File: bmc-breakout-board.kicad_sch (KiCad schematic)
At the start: 9 parts

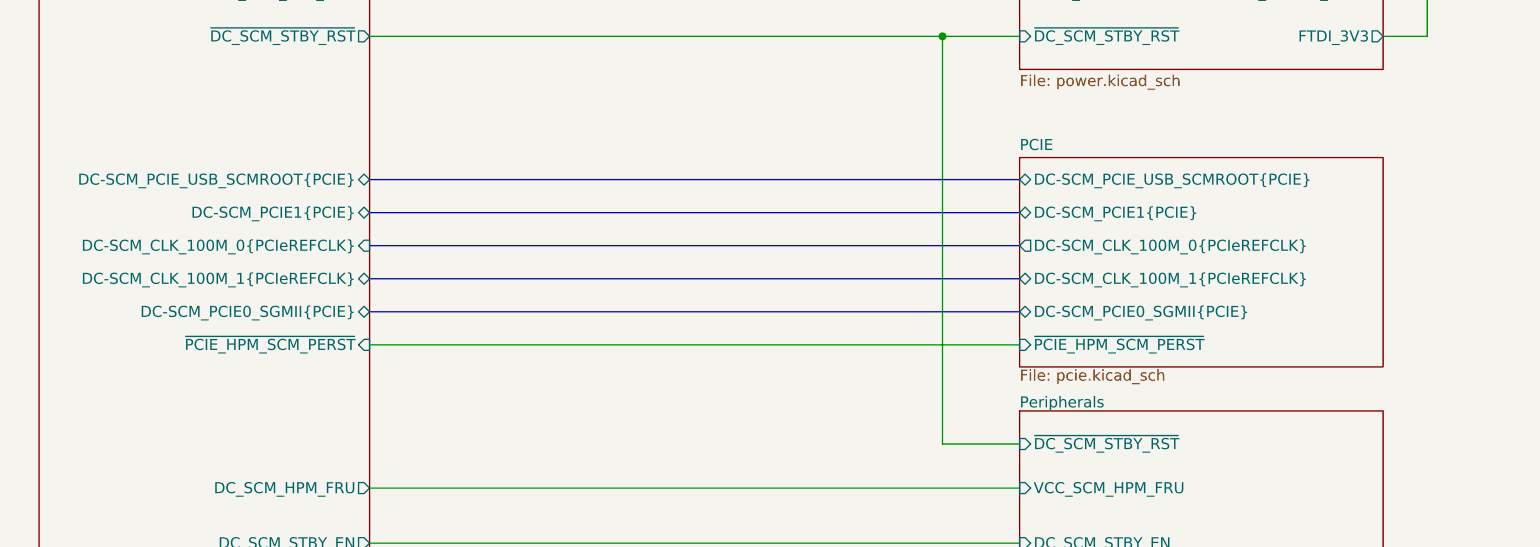
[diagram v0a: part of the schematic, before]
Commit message: [#93514] Remove unnecessary PCIE testpads
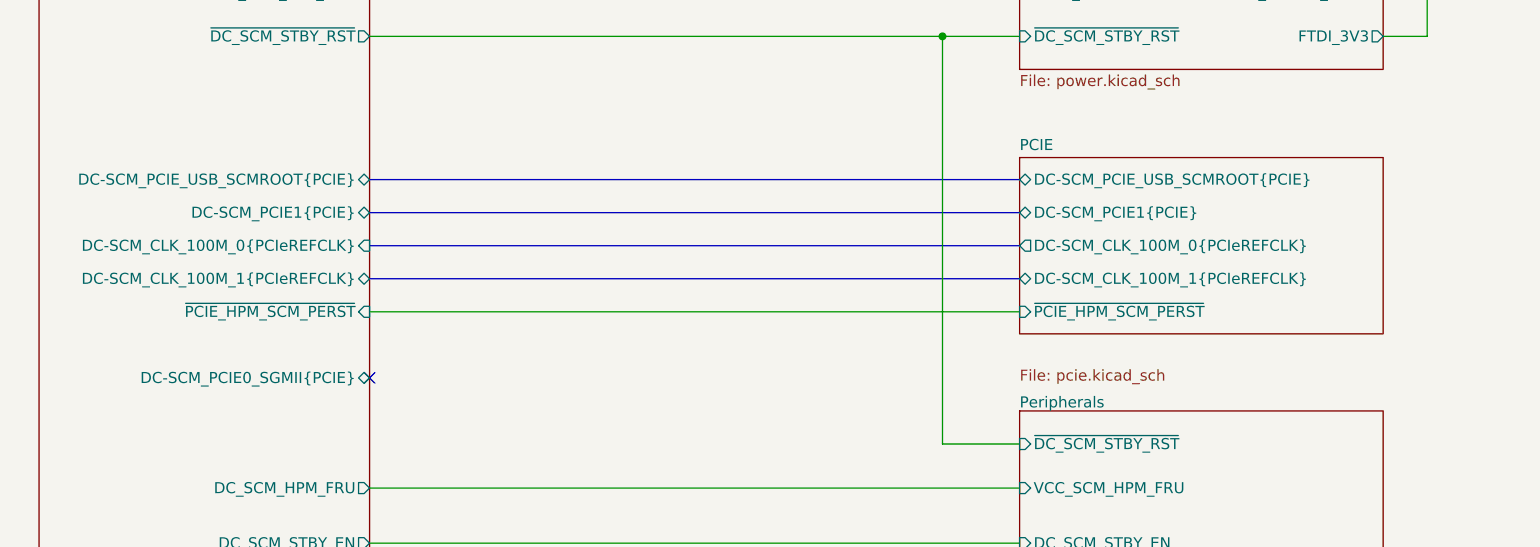
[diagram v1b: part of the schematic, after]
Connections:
- no-connect marks 0 -> 1
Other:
- sheet PCIE ports: added none; removed DC-SCM_PCIE0_SGMII{PCIE}
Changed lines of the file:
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@@
 		(color 0 0 0 0)
 	)
+	(no_connect
+		(at 81.28 102.87)
+	)
 	(wire
 		(pts
@@
 	(bus
 		(pts
-			(xy 81.28 95.25) (xy 156.21 95.25)
-		)
-		(stroke
-			(width 0)
-			(type default)
-		)
-	)
-	(bus
-		(pts
 			(xy 81.28 228.6) (xy 156.21 228.6)
 		)
@@
 	(wire
 		(pts
-			(xy 81.28 99.06) (xy 156.21 99.06)
+			(xy 81.28 95.25) (xy 156.21 95.25)
 		)
 		(stroke
@@
 	(sheet
 		(at 156.21 77.47)
-		(size 41.91 24.13)
+		(size 41.91 20.32)
 		(exclude_from_sim no)
 		(in_bom yes)
@@
 			)
 		)
-		(pin "DC-SCM_PCIE0_SGMII{PCIE}" bidirectional
-			(at 156.21 95.25 180)
-			(effects
-				(font
-					(size 1.27 1.27)
-				)
-				(justify left)
-			)
-		)
 		(pin "~{PCIE_HPM_SCM_PERST}" input
-			(at 156.21 99.06 180)
+			(at 156.21 95.25 180)
 			(effects
 				(font
@@
 		)
 		(pin "DC-SCM_PCIE0_SGMII{PCIE}" bidirectional
-			(at 81.28 95.25 0)
+			(at 81.28 102.87 0)
 			(effects
 				(font
@@
 		)
 		(pin "~{PCIE_HPM_SCM_PERST}" input
-			(at 81.28 99.06 0)
+			(at 81.28 95.25 0)
 			(effects
 				(font

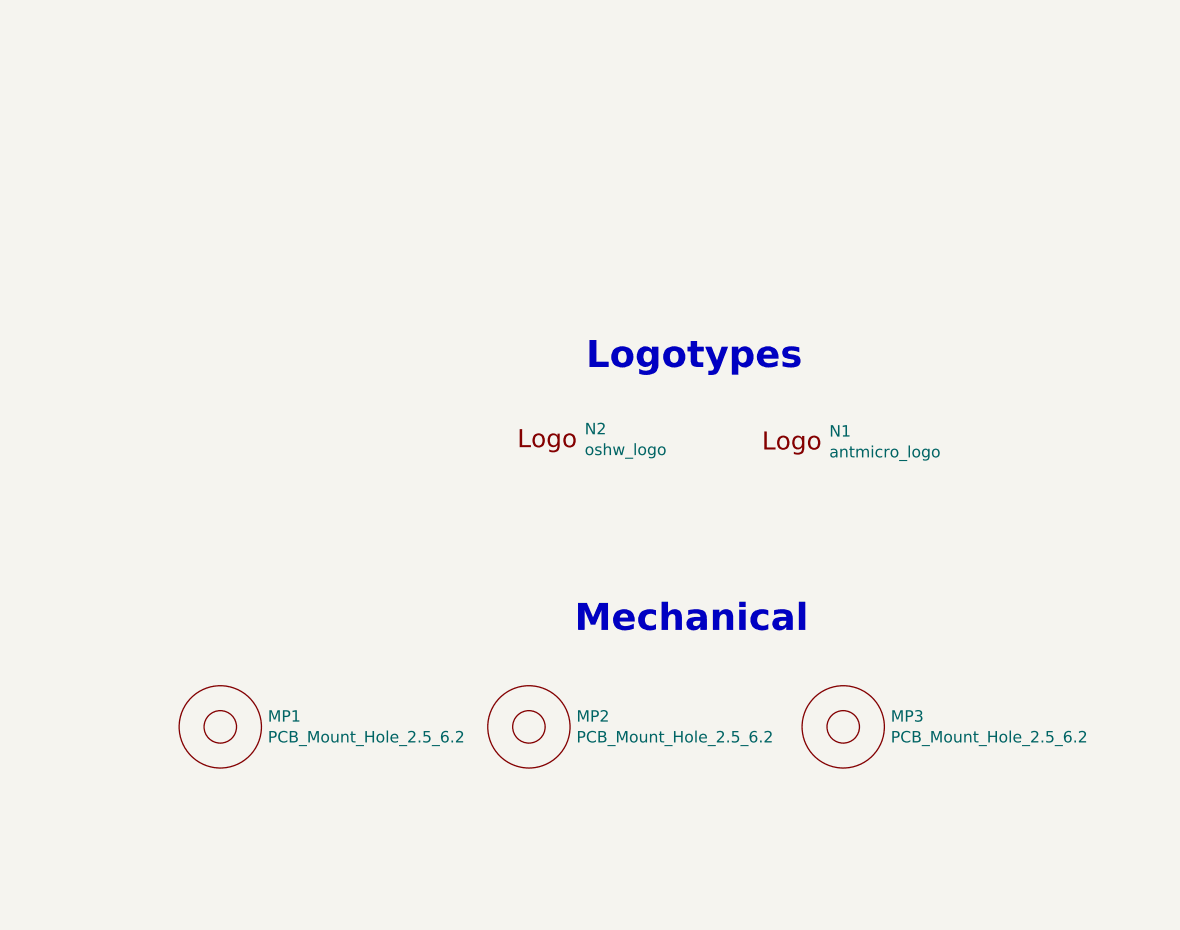
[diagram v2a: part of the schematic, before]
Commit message: [#93949] Add fiducials and 4th mounting hole
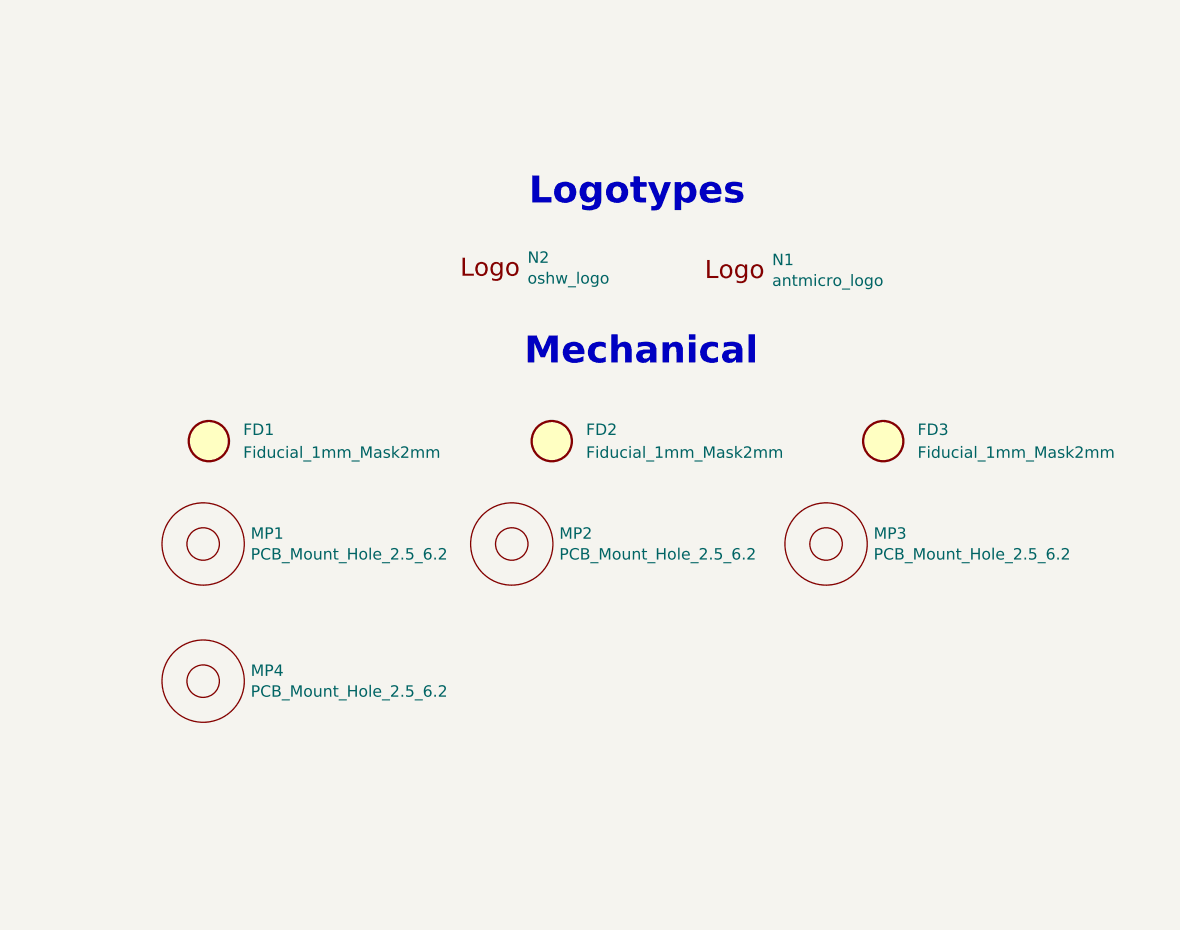
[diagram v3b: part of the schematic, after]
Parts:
- added FD1, FD2, FD3: Fiducial_1mm_Mask2mm, antmicro-footprints:Fiducial_1mm_Mask2mm, symbol antmicroFiducialMarks:Fiducial_1mm_Mask2mm
- added MP4: PCB_Mount_Hole_2.5_6.2, antmicro-footprints:MP_Pad5.5mm_Drill2.9mm, symbol bmc-breakout-board:PCB_Mount_Hole_2.5_6.2
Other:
- moved on the sheet: MP1, MP2, MP3, N1, N2

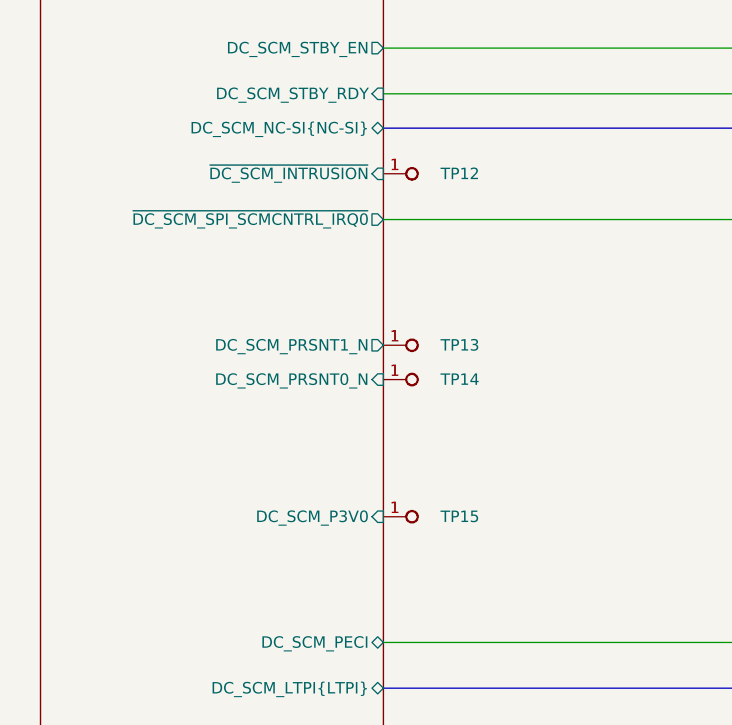
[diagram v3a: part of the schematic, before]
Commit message: [#93949] Change testpads to 1.5mm, change QSPI and UART testpad to smd technology
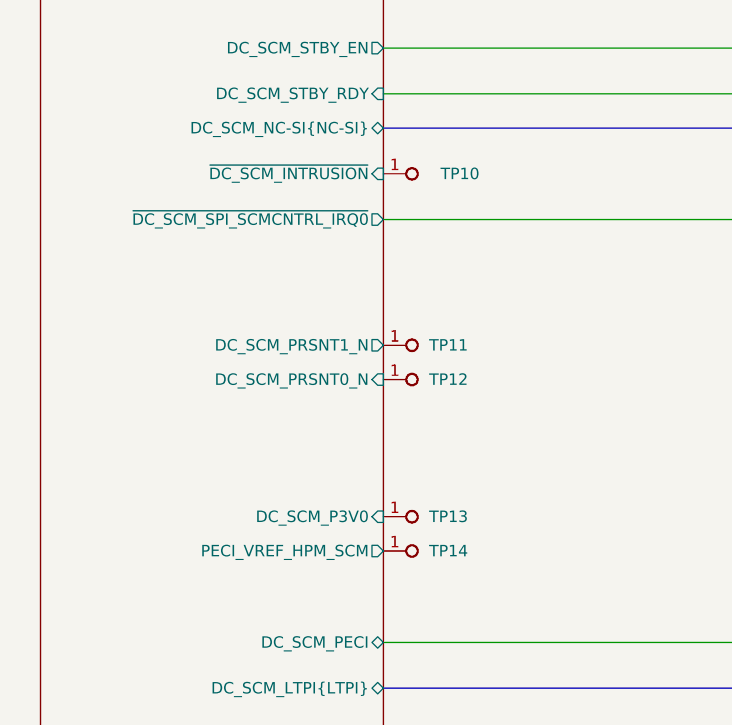
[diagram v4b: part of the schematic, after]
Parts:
- removed TP12, TP13, TP14, TP15: TP_0.75mm_SMD, antmicro-footprints:TP_SMD_0.75mm, symbol antmicroTestPoints:TP_0.75mm_SMD
- added TP10, TP11, TP12, TP13, TP14: TP_1.5mm_SMD, antmicro-footprints:TP_SMD_1.5mm, symbol antmicroTestPoints:TP_1.5mm_SMD
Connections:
- net DC-SCM 2.1 connector/DC_SCM_P3V0: now also TP13.1
- net DC-SCM 2.1 connector/DC_SCM_PRSNT0_N: now also TP12.1
- net DC-SCM 2.1 connector/DC_SCM_PRSNT1_N: now also TP11.1
- net DC-SCM 2.1 connector/~{DC_SCM_INTRUSION}: now also TP10.1
- new net DC-SCM 2.1 connector/PECI_VREF_HPM_SCM: TP14.1
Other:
- sheet DC-SCM 2.1 connector ports: added PECI_VREF_HPM_SCM; removed none

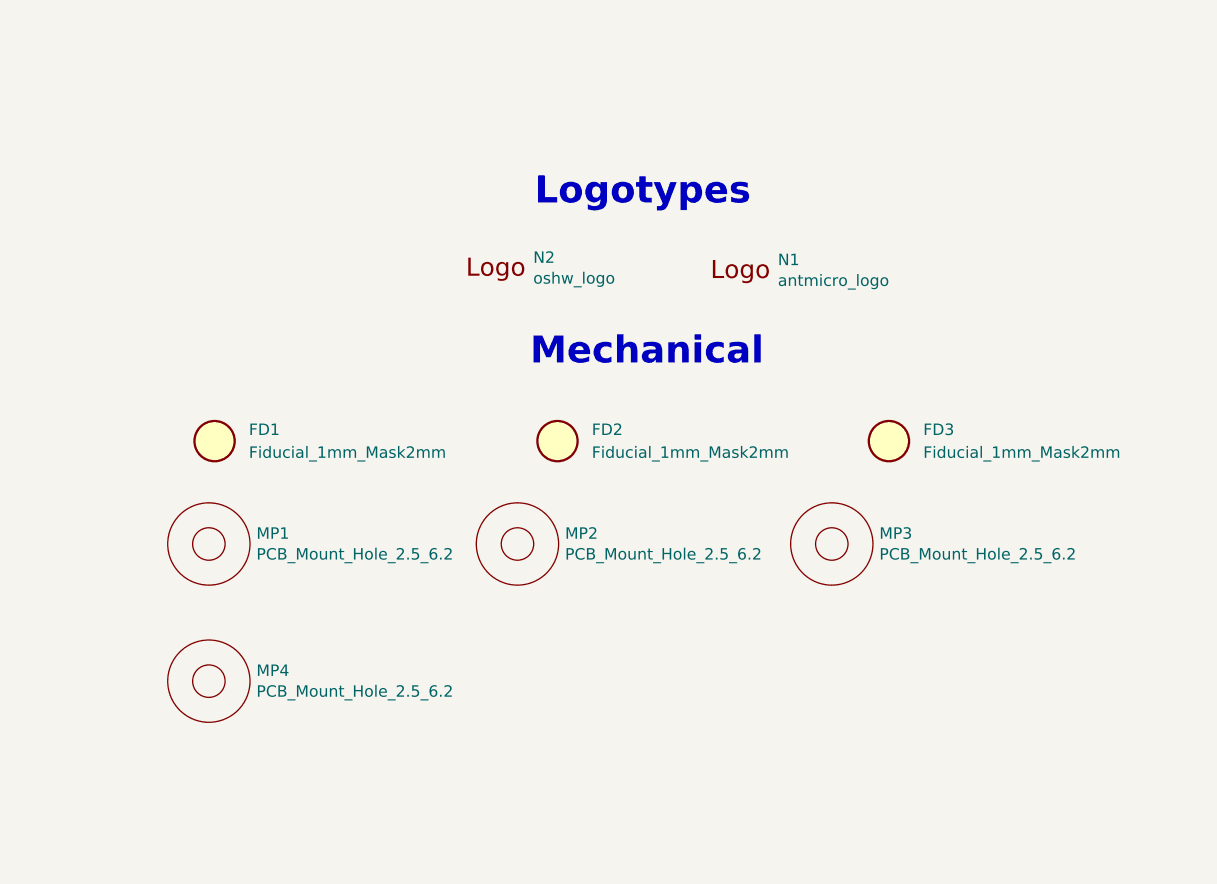
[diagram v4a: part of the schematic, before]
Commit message: [#93949] Align items to grid, change TP for UART
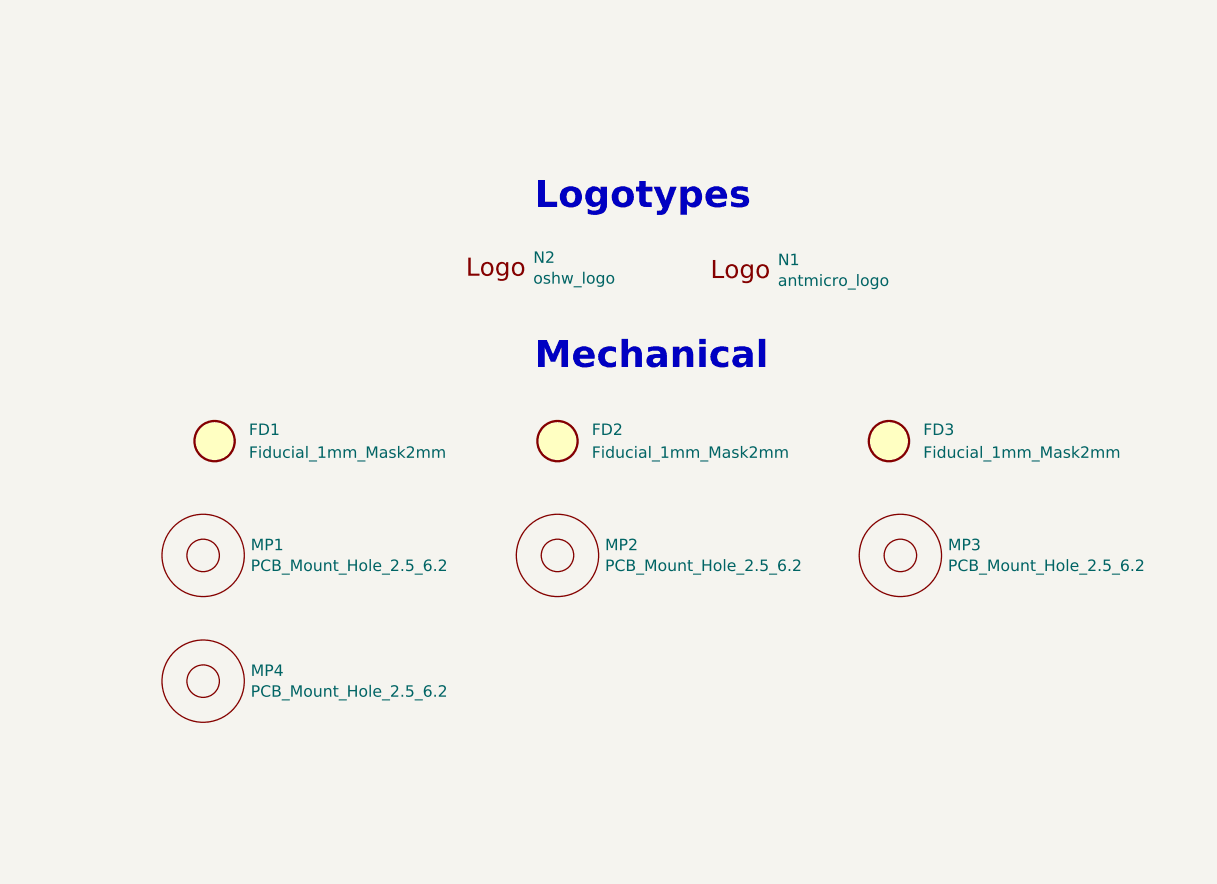
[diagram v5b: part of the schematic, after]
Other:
- moved on the sheet: MP4

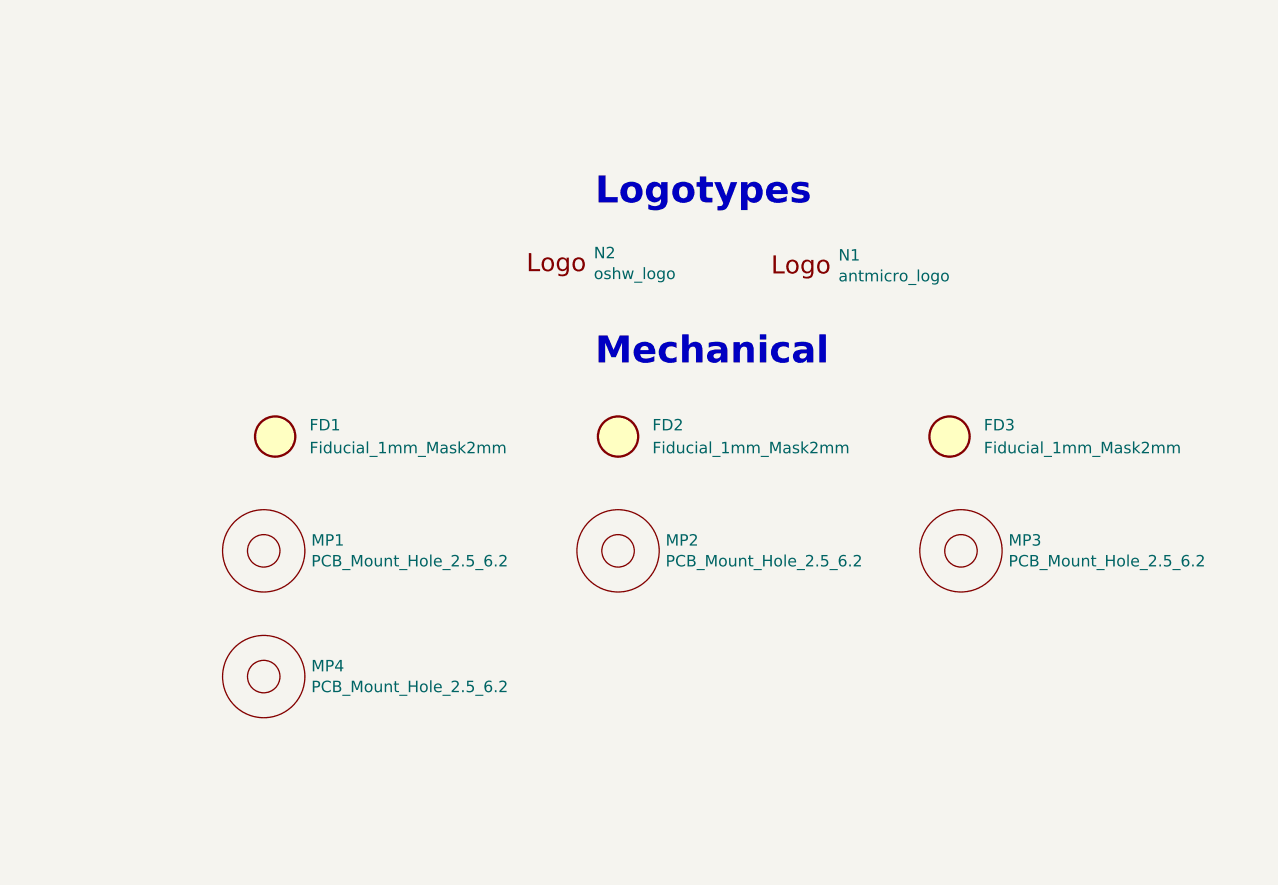
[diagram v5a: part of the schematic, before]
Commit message: [#93949] Change mechanical pads to ones with GND
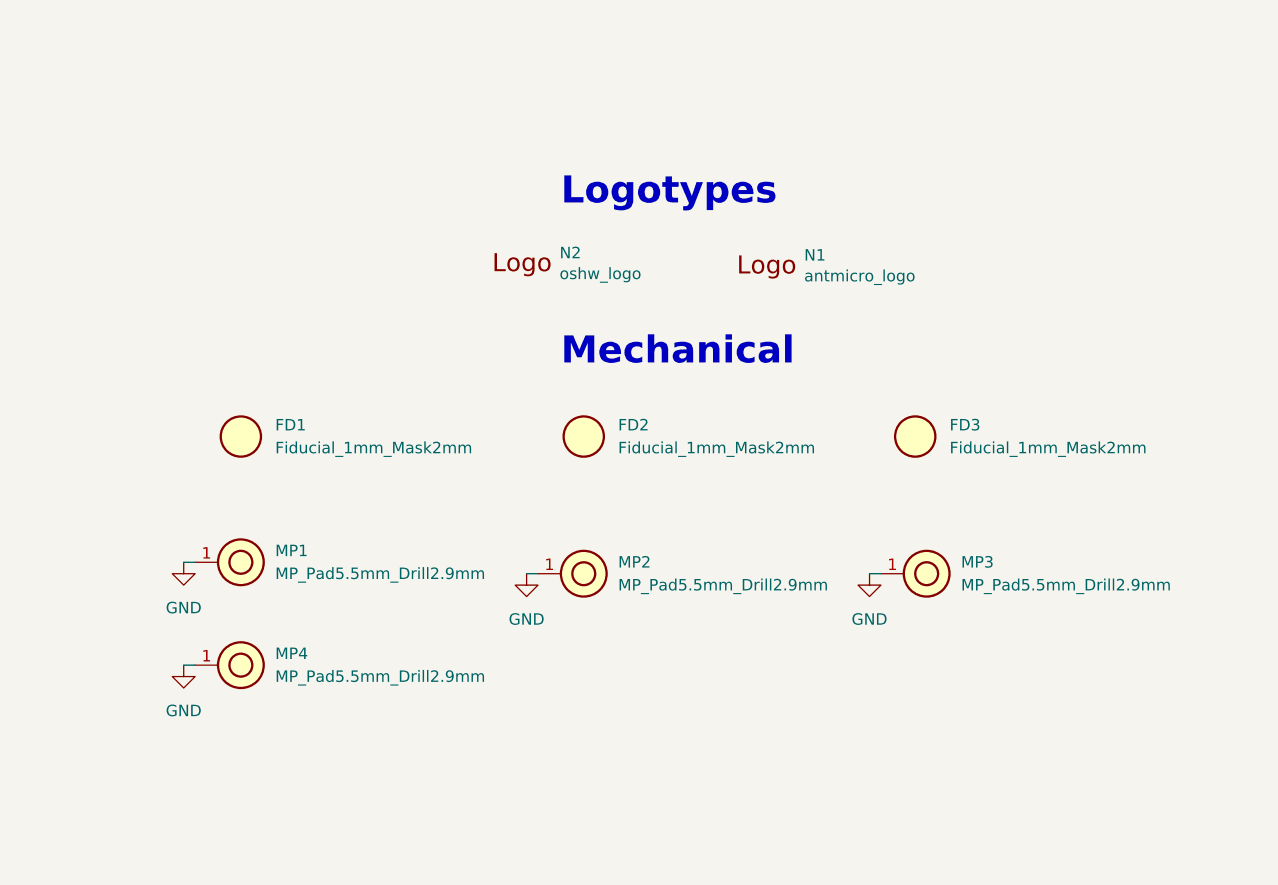
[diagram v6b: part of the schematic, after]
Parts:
- removed MP1, MP2, MP3, MP4: PCB_Mount_Hole_2.5_6.2, antmicro-footprints:MP_Pad5.5mm_Drill2.9mm, symbol bmc-breakout-board:PCB_Mount_Hole_2.5_6.2
- added MP1, MP2, MP3, MP4: MP_Pad5.5mm_Drill2.9mm, antmicro-footprints:MP_Pad5.5mm_Drill2.9mm, symbol antmicroMechanicalParts:MP_Pad5.5mm_Drill2.9mm
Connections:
- new net GND: MP1.1, MP2.1, MP3.1, MP4.1
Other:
- moved on the sheet: FD1, FD2, FD3, N1, N2
